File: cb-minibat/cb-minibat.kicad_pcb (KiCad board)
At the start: 4 copper layers, 25.4 x 56.6 mm, 24 parts, among them P1 CONN_01X14, P2 CONN_01X14, SW1 SW_PUSH, U1 BMP180, U2 MMA8652FC, U3 SI7021, U4 ANTENNA

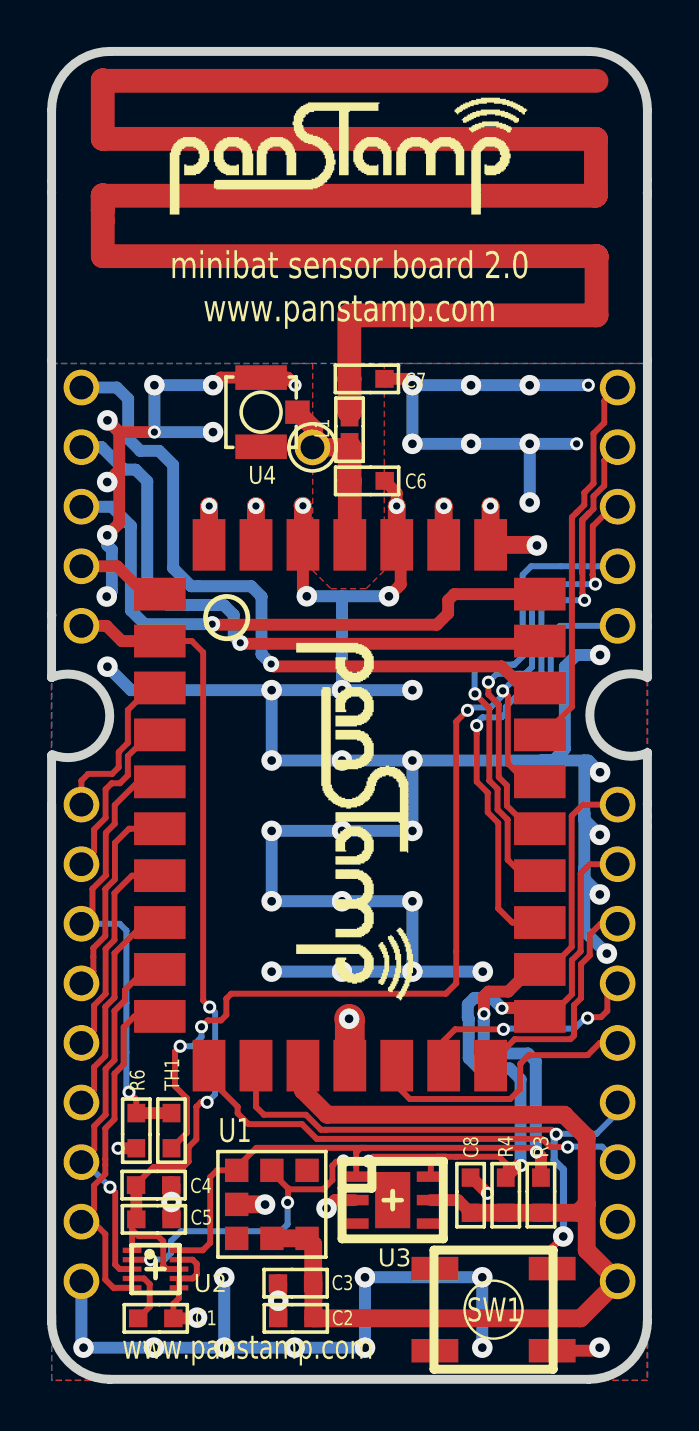
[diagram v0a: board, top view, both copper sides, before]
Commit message: New version 2.1 with support for BME680
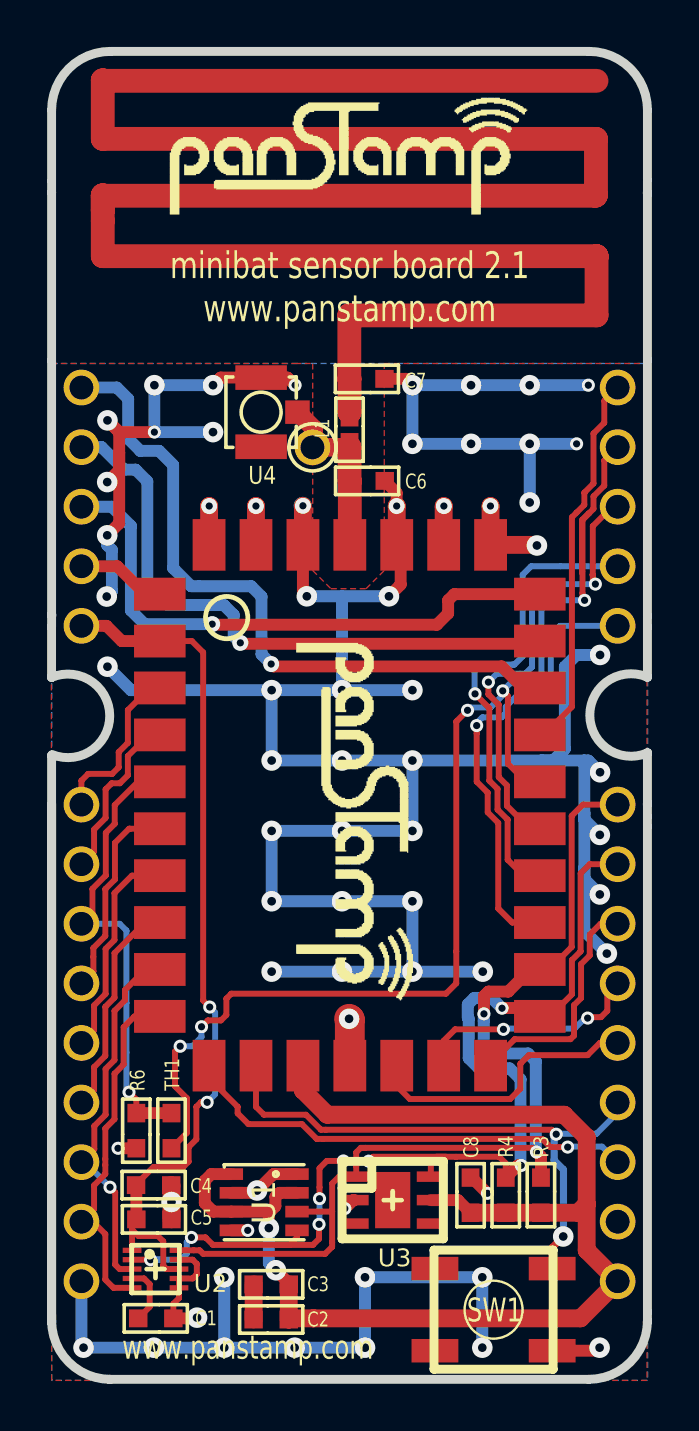
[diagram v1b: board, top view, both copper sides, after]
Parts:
- U1: value BMP180 -> BME680; footprint mysmd:BMP180 -> mysmd:BME680
- moved C2 1.05 mm to (125.0, 99.8)
- moved C3 1.04 mm to (125.0, 98.3)
- moved U1 0.34 mm to (124.7, 94.8)
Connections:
- U1 pad 1: (no net) -> GND
- U1 pad 3: VCC -> /I2C_SDA
- U1 pad 4: (no net) -> /I2C_SCL
- U1 pad 5: /I2C_SCL -> GND
- U1 pad 6: /I2C_SDA -> VCC
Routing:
- net VCC: track 46.4 -> 54.4 mm, vias 0 -> 2
- net GND: track 192.3 -> 194.1 mm
- net /I2C_SCL: track 44.6 -> 45.9 mm, vias 6 -> 8
- net /I2C_SDA: track 43.7 -> 44.2 mm
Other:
- board text added: "minibat sensor board 2.1 www.panstamp.com"
- board text removed: "minibat sensor board 2.0 www.panstamp.com"
